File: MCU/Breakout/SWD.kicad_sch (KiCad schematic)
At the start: 1 part, among them J1 Conn_01x05_Male_Programmer

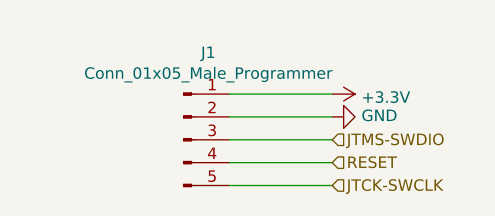
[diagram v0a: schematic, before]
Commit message: Renamed SWD to remove space from name
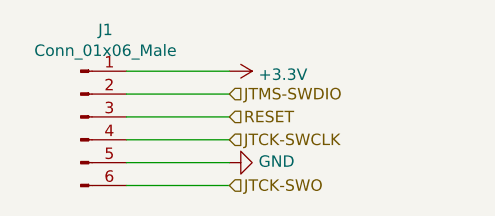
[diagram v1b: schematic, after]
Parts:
- removed J1: Conn_01x05_Male_Programmer, Connector_PinHeader_2.54mm:PinHeader_1x05_P2.54mm_Vertical, symbol Connector:Conn_01x05_Male
- added J1: Conn_01x06_Male, NOVA MCU (STM):j-link_6_pin_needle, symbol Connector:Conn_01x06_Male
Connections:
- net +3V3: now also J1.1 (Pin_1)
- net GND: now also J1.5 (Pin_5)
- net JTCK-SWCLK: now also J1.4 (Pin_4)
- net JTMS-SWDIO: now also J1.2 (Pin_2)
- net RESET: now also J1.3 (Pin_3)
- new net JTCK-SWO: J1.6 (Pin_6)
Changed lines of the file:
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@@
     (rev "1")
   )
-  (wire (pts (xy 146.05 91.44) (xy 157.48 91.44))
+  (wire (pts (xy 134.62 93.98) (xy 146.05 93.98))
     (stroke (width 0) (type default) (color 0 0 0 0))
   )
-  (wire (pts (xy 146.05 93.98) (xy 157.48 93.98))
+  (wire (pts (xy 134.62 101.6) (xy 146.05 101.6))
     (stroke (width 0) (type default) (color 0 0 0 0))
   )
-  (wire (pts (xy 146.05 99.06) (xy 157.48 99.06))
+  (wire (pts (xy 134.62 88.9) (xy 146.05 88.9))
     (stroke (width 0) (type default) (color 0 0 0 0))
   )
-  (wire (pts (xy 146.05 101.6) (xy 157.48 101.6))
+  (wire (pts (xy 134.62 99.06) (xy 146.05 99.06))
     (stroke (width 0) (type default) (color 0 0 0 0))
   )
-  (wire (pts (xy 146.05 96.52) (xy 157.48 96.52))
+  (wire (pts (xy 134.62 91.44) (xy 146.05 91.44))
+    (stroke (width 0) (type default) (color 0 0 0 0))
+  )
+  (wire (pts (xy 134.62 96.52) (xy 146.05 96.52))
     (stroke (width 0) (type default) (color 0 0 0 0))
   )
@@
     )
   )
-  (hierarchical_label "JTCK-SWCLK" (shape input) (at 157.48 101.6 0)
+  (hierarchical_label "JTCK-SWCLK" (shape input) (at 146.05 96.52 0)
     (effects (font (size 1.27 1.27)) (justify left))
   )
-  (hierarchical_label "RESET" (shape input) (at 157.48 99.06 0)
+  (hierarchical_label "JTMS-SWDIO" (shape input) (at 146.05 91.44 0)
     (effects (font (size 1.27 1.27)) (justify left))
   )
-  (hierarchical_label "JTMS-SWDIO" (shape input) (at 157.48 96.52 0)
+  (hierarchical_label "RESET" (shape input) (at 146.05 93.98 0)
     (effects (font (size 1.27 1.27)) (justify left))
   )
-  (symbol (lib_id "power:+3.3V") (at 157.48 91.44 270) (unit 1)
+  (hierarchical_label "JTCK-SWO" (shape input) (at 146.05 101.6 0)
+    (effects (font (size 1.27 1.27)) (justify left))
+  )
+  (symbol (lib_id "Connector:Conn_01x06_Male") (at 129.54 93.98 0) (unit 1)
     (in_bom yes) (on_board yes)
-    (property "Reference" "#PWR09" (id 0) (at 153.67 91.44 0)
-      (effects (font (size 1.27 1.27)) hide)
-    )
-    (property "Value" "+3.3V" (id 1) (at 160.7312 91.821 90)
-      (effects (font (size 1.27 1.27)) (justify left))
-    )
-    (property "Footprint" "" (id 2) (at 157.48 91.44 0)
-      (effects (font (size 1.27 1.27)) hide)
-    )
-    (property "Datasheet" "" (id 3) (at 157.48 91.44 0)
-      (effects (font (size 1.27 1.27)) hide)
-    )
-    (pin "1")
-  )
-  (symbol (lib_id "power:GND") (at 157.48 93.98 90) (unit 1)
-    (in_bom yes) (on_board yes)
-    (property "Reference" "#PWR010" (id 0) (at 163.83 93.98 0)
-      (effects (font (size 1.27 1.27)) hide)
-    )
-    (property "Value" "GND" (id 1) (at 160.7312 93.853 90)
-      (effects (font (size 1.27 1.27)) (justify right))
-    )
-    (property "Footprint" "" (id 2) (at 157.48 93.98 0)
-      (effects (font (size 1.27 1.27)) hide)
-    )
-    (property "Datasheet" "" (id 3) (at 157.48 93.98 0)
-      (effects (font (size 1.27 1.27)) hide)
-    )
-    (pin "1")
-  )
-  (symbol (lib_id "Connector:Conn_01x05_Male") (at 140.97 96.52 0) (unit 1)
-    (in_bom yes) (on_board yes)
-    (property "Reference" "J1" (id 0) (at 143.7132 86.8426 0))
-    (property "Value" "Conn_01x05_Male_Programmer" (id 1) (at 143.7132 89.154 0))
-    (property "Footprint" "Connector_PinHeader_2.54mm:PinHeader_1x05_P2.54mm_Vertical" (id 2) (at 140.97 96.52 0)
-      (effects (font (size 1.27 1.27)) hide)
-    )
-    (property "Datasheet" "~" (id 3) (at 140.97 96.52 0)
+    (property "Reference" "J1" (id 0) (at 132.2832 84.3026 0))
+    (property "Value" "Conn_01x06_Male" (id 1) (at 132.2832 86.614 0))
+    (property "Footprint" "NOVA MCU (STM):j-link_6_pin_needle" (id 2) (at 129.54 93.98 0)
+      (effects (font (size 1.27 1.27)) hide)
+    )
+    (property "Datasheet" "~" (id 3) (at 129.54 93.98 0)
       (effects (font (size 1.27 1.27)) hide)
     )
@@
     (pin "4")
     (pin "5")
+    (pin "6")
+  )
+  (symbol (lib_id "power:GND") (at 146.05 99.06 90) (unit 1)
+    (in_bom yes) (on_board yes)
+    (property "Reference" "#PWR0163" (id 0) (at 152.4 99.06 0)
+      (effects (font (size 1.27 1.27)) hide)
+    )
+    (property "Value" "GND" (id 1) (at 149.3012 98.933 90)
+      (effects (font (size 1.27 1.27)) (justify right))
+    )
+    (property "Footprint" "" (id 2) (at 146.05 99.06 0)
+      (effects (font (size 1.27 1.27)) hide)
+    )
+    (property "Datasheet" "" (id 3) (at 146.05 99.06 0)
+      (effects (font (size 1.27 1.27)) hide)
+    )
+    (pin "1")
+  )
+  (symbol (lib_id "power:+3.3V") (at 146.05 88.9 270) (unit 1)
+    (in_bom yes) (on_board yes)
+    (property "Reference" "#PWR0124" (id 0) (at 142.24 88.9 0)
+      (effects (font (size 1.27 1.27)) hide)
+    )
+    (property "Value" "+3.3V" (id 1) (at 149.3012 89.281 90)
+      (effects (font (size 1.27 1.27)) (justify left))
+    )
+    (property "Footprint" "" (id 2) (at 146.05 88.9 0)
+      (effects (font (size 1.27 1.27)) hide)
+    )
+    (property "Datasheet" "" (id 3) (at 146.05 88.9 0)
+      (effects (font (size 1.27 1.27)) hide)
+    )
+    (pin "1")
   )
 )
